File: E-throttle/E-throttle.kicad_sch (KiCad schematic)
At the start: 34 parts, among them J1 PROG, J2 JTAG, J3 Conn_01x11, J4 Conn_01x11, J5 776087-1, Q1 NMOS, SW1 SW_Push, U1 ESP32-S3-WROOM-1-N16R8, U2 LM317_SOT-223, U3 LM317_SOT-223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

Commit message: Completed wiring 2.0
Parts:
- added H1, H2, H3, H4: MountingHole_Pad, MountingHole:MountingHole_3.2mm_M3_Pad_Via, symbol Mechanical:MountingHole_Pad
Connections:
- net CAN-H: now also J5.16 (Pin_16); no longer J5.19 (Pin_19)
- net CAN-L: now also J5.17 (Pin_17); no longer J5.20 (Pin_20)
- net GND: now also J5.15 (Pin_15), J5.18 (Pin_18), J5.19 (Pin_19), H1.1, H2.1, H3.1, H4.1; no longer J5.21 (Pin_21), J5.22 (Pin_22), J5.23 (Pin_23)
- net STEP-1+: now also J5.20 (Pin_20); no longer J5.15 (Pin_15)
- net STEP-1-: now also J5.21 (Pin_21); no longer J5.16 (Pin_16)
- net STEP-2+: now also J5.22 (Pin_22); no longer J5.17 (Pin_17)
- net STEP-2-: now also J5.23 (Pin_23); no longer J5.18 (Pin_18)

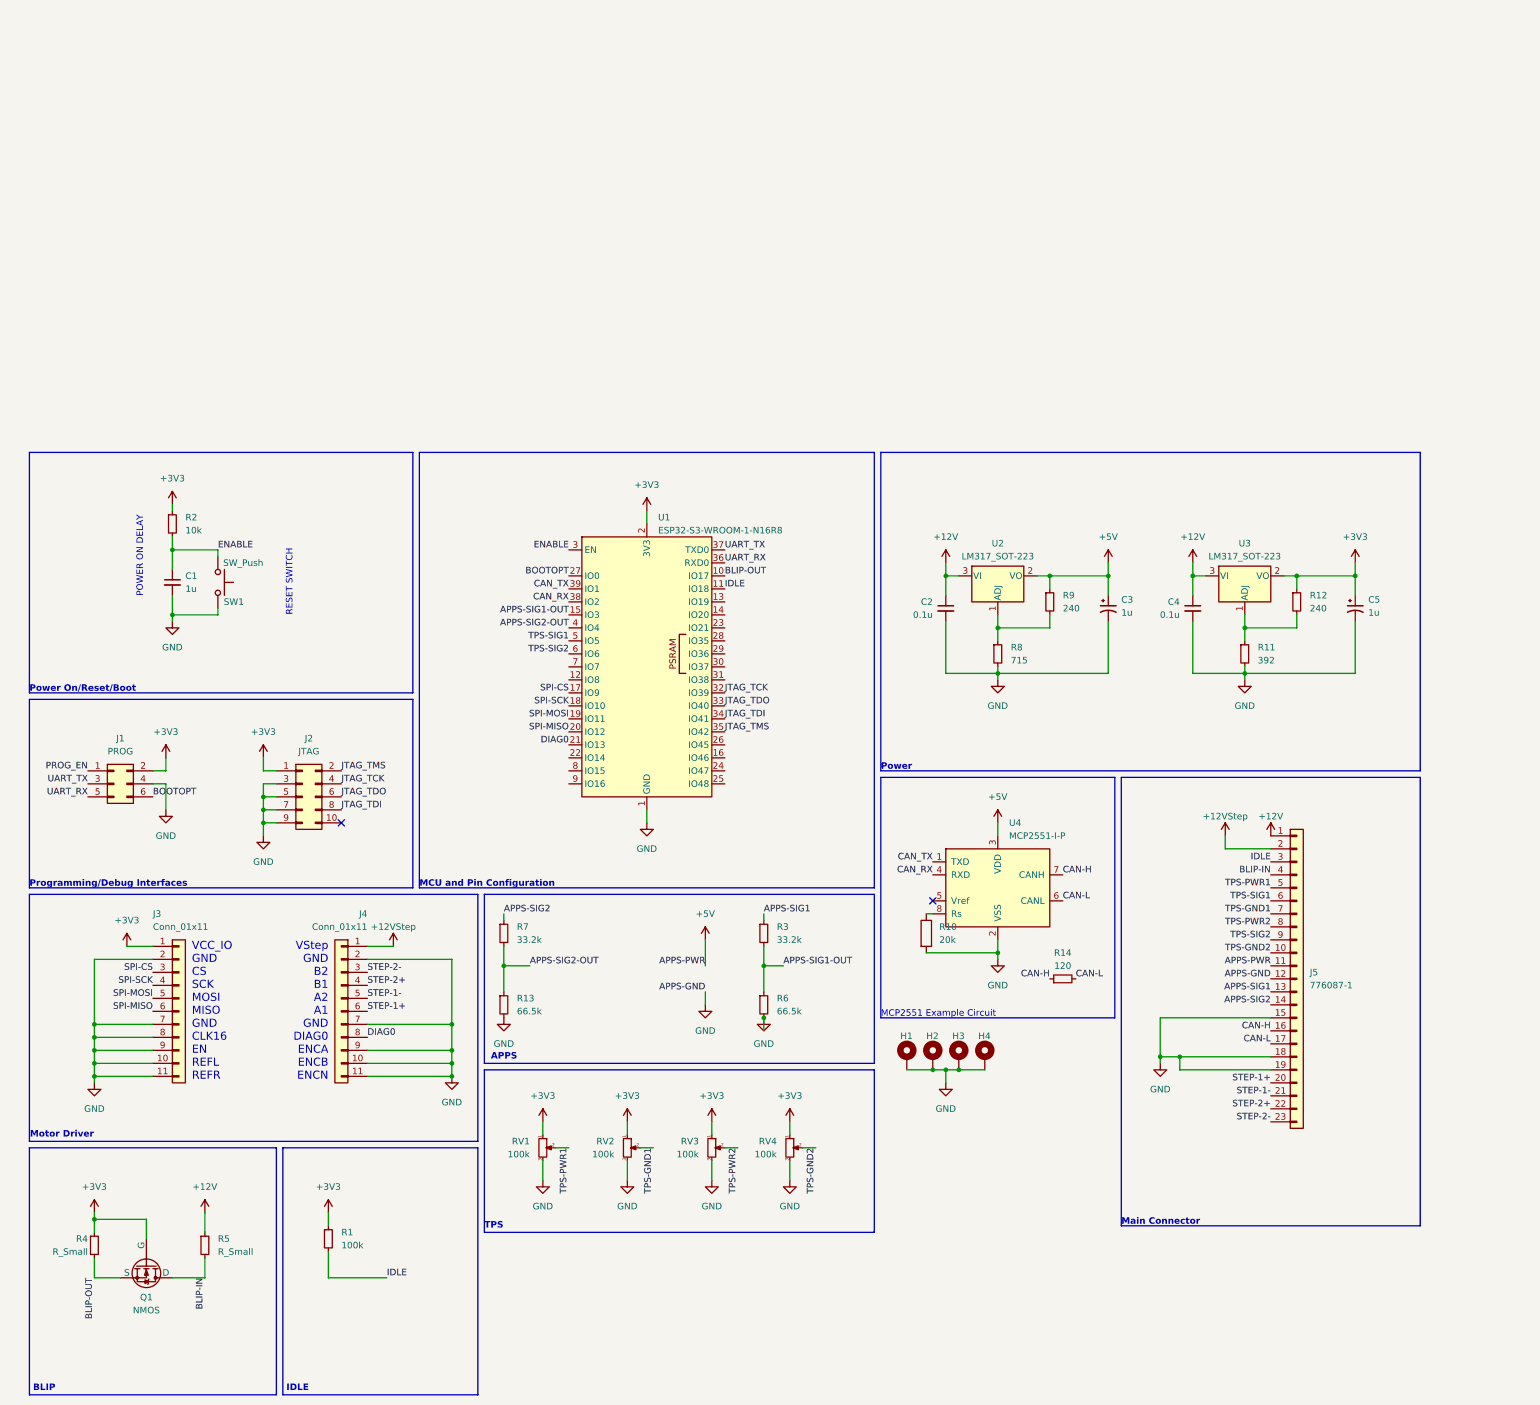
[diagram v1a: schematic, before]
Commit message: Updated PCB for 2026 (v0.1)
- Switch from ESP32 S3 Wroom1 Module to ESP dev board (Todo: Check Power Supply to ESP32 and other components)
- Fixed incorrect TPS wiring (replaced variable resistors)
- Did not reconnect JTAG debugger and programmer to ESP32 Dev Board
- Did not reconnect CAN Transceiver

Co-Authored-By: Clement Tong (Yuk Chun) <clement.yc.tong@gmail.com>
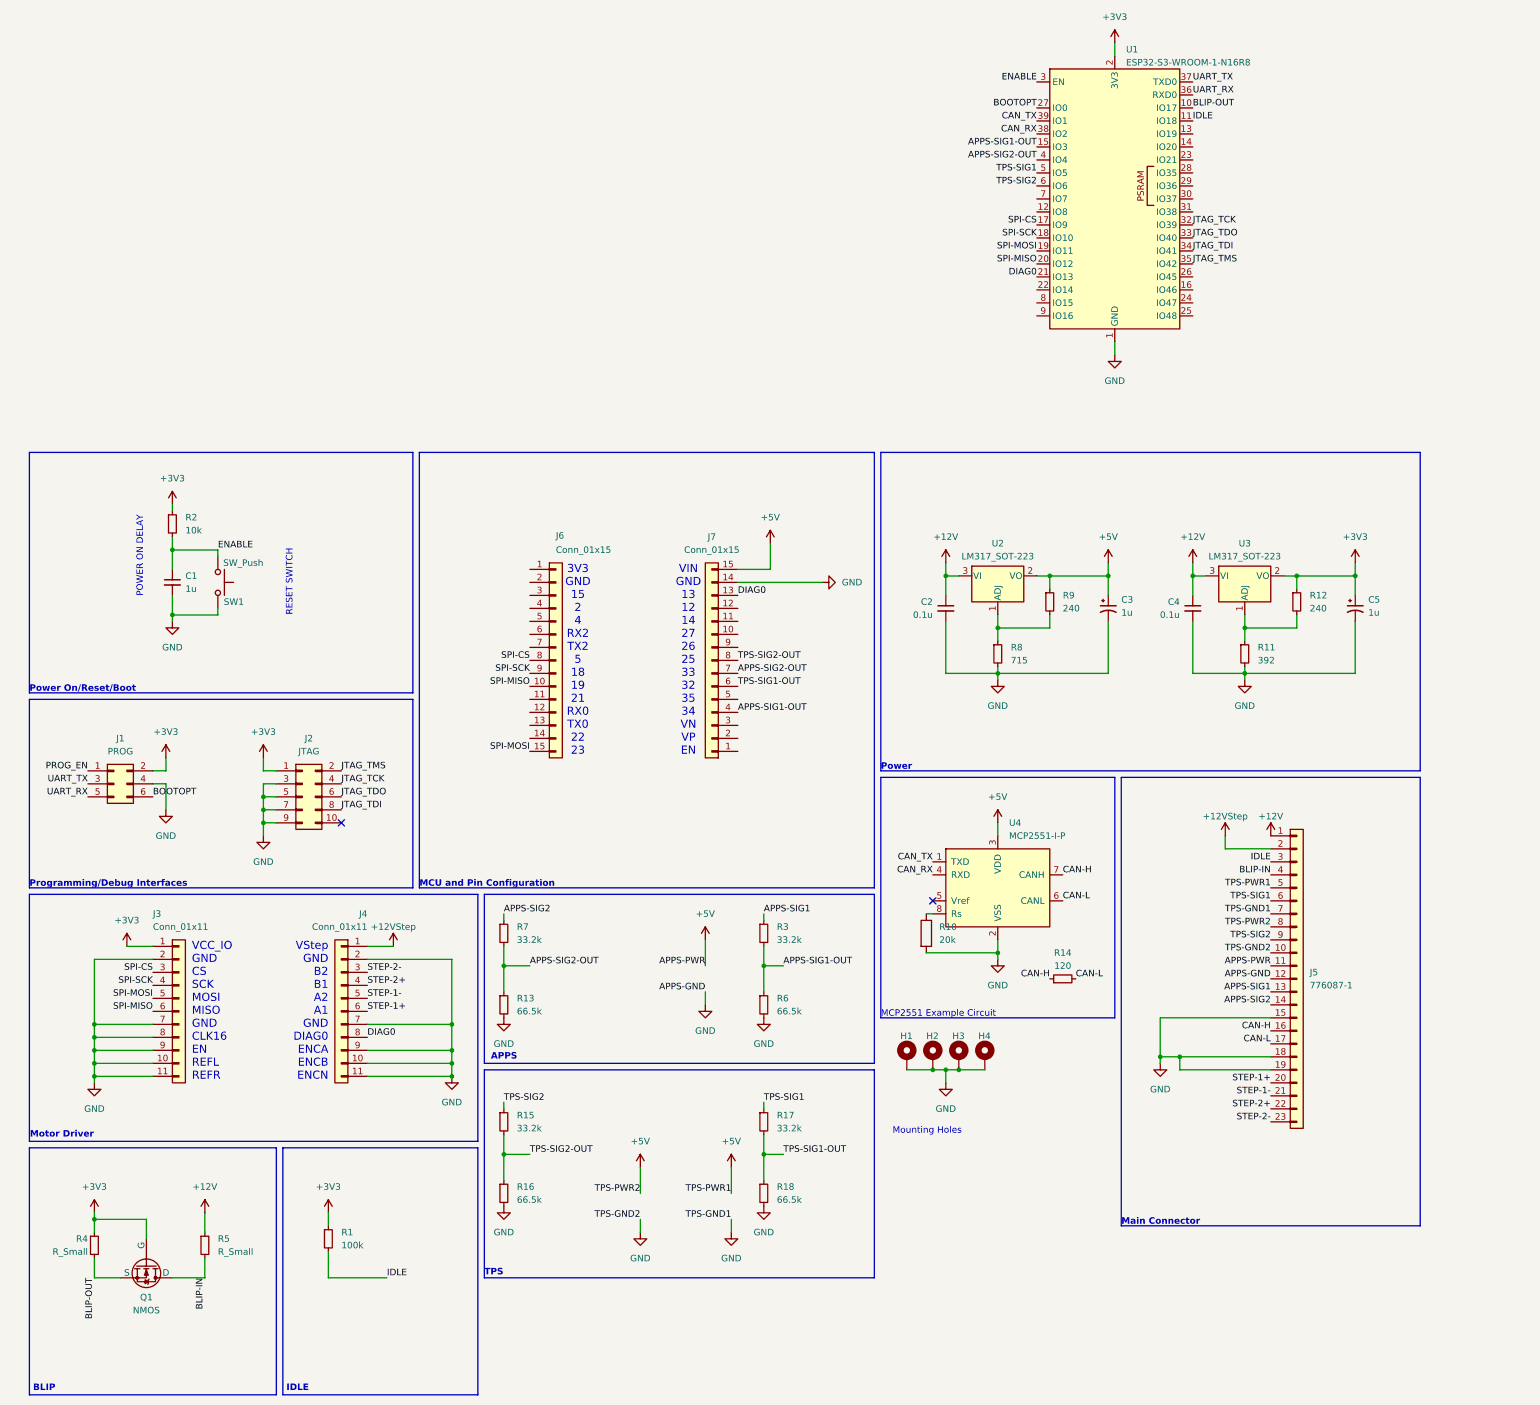
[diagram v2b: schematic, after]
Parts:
- removed RV1, RV2, RV3, RV4: 100k, Potentiometer_THT:Potentiometer_Bourns_3296Y_Vertical, symbol Device:R_Potentiometer_Small
- added J6, J7: Conn_01x15, symbol Connector_Generic:Conn_01x15
- added R15, R17: 33.2k, Resistor_THT:R_Axial_DIN0207_L6.3mm_D2.5mm_P10.16mm_Horizontal, symbol Device:R_Small
- added R16, R18: 66.5k, Resistor_THT:R_Axial_DIN0207_L6.3mm_D2.5mm_P10.16mm_Horizontal, symbol Device:R_Small
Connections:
- net TPS-GND1 is gone; now on net GND: J5.7 (Pin_7)
- net TPS-GND2 is gone; now on net GND: J5.10 (Pin_10)
- net TPS-PWR1 is gone; now on net +5V: J5.5 (Pin_5)
- net TPS-PWR2 is gone; now on net +5V: J5.8 (Pin_8)
- net +5V: now also J7.15 (Pin_15)
- net APPS-SIG1-OUT: now also J7.4 (Pin_4)
- net APPS-SIG2-OUT: now also J7.7 (Pin_7)
- net DIAG0: now also J7.13 (Pin_13)
- net GND: now also J7.14 (Pin_14), R16.2, R18.2
- net SPI-CS: now also J6.8 (Pin_8)
- net SPI-MISO: now also J6.10 (Pin_10)
- net SPI-MOSI: now also J6.15 (Pin_15)
- net SPI-SCK: now also J6.9 (Pin_9)
- net TPS-SIG1: now also R17.1
- net TPS-SIG2: now also R15.1
- new net TPS-SIG1-OUT: J7.6 (Pin_6), R17.2, R18.1
- new net TPS-SIG2-OUT: J7.8 (Pin_8), R15.2, R16.1
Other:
- note added: "3V3 GND 15 2 4 RX2 TX2 5 18 19 21 RX0 TX0 22 23"
- note added: "Mounting Holes"
- note added: "VIN GND 13 12 14 27 26 25 33 32 35 34 VN VP EN"
- moved on the sheet: U1

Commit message: Implemented Level 1 Failure Circuit
- Added Hardware Watchdog (74HC123) that requires ESP32 to send "Heartbeat" alive signal every 20ms, or else the stepper motor power gets cut

- ⁠Added PROFET / Automotive Smart High-Side Switch (BTS441TG) to cut power to the stepper motor, if the hardware watchdog doesn't receive a heartbeat from the ESP32 within the required timeframe (We set this hardware timeout to 50ms to comply with the FSUK rule CV1.6.4 that requires motor power to be cut if plausibility fails for more than 100ms)

Co-Authored-By: Clement Tong (Yuk Chun) <clement.yc.tong@gmail.com>
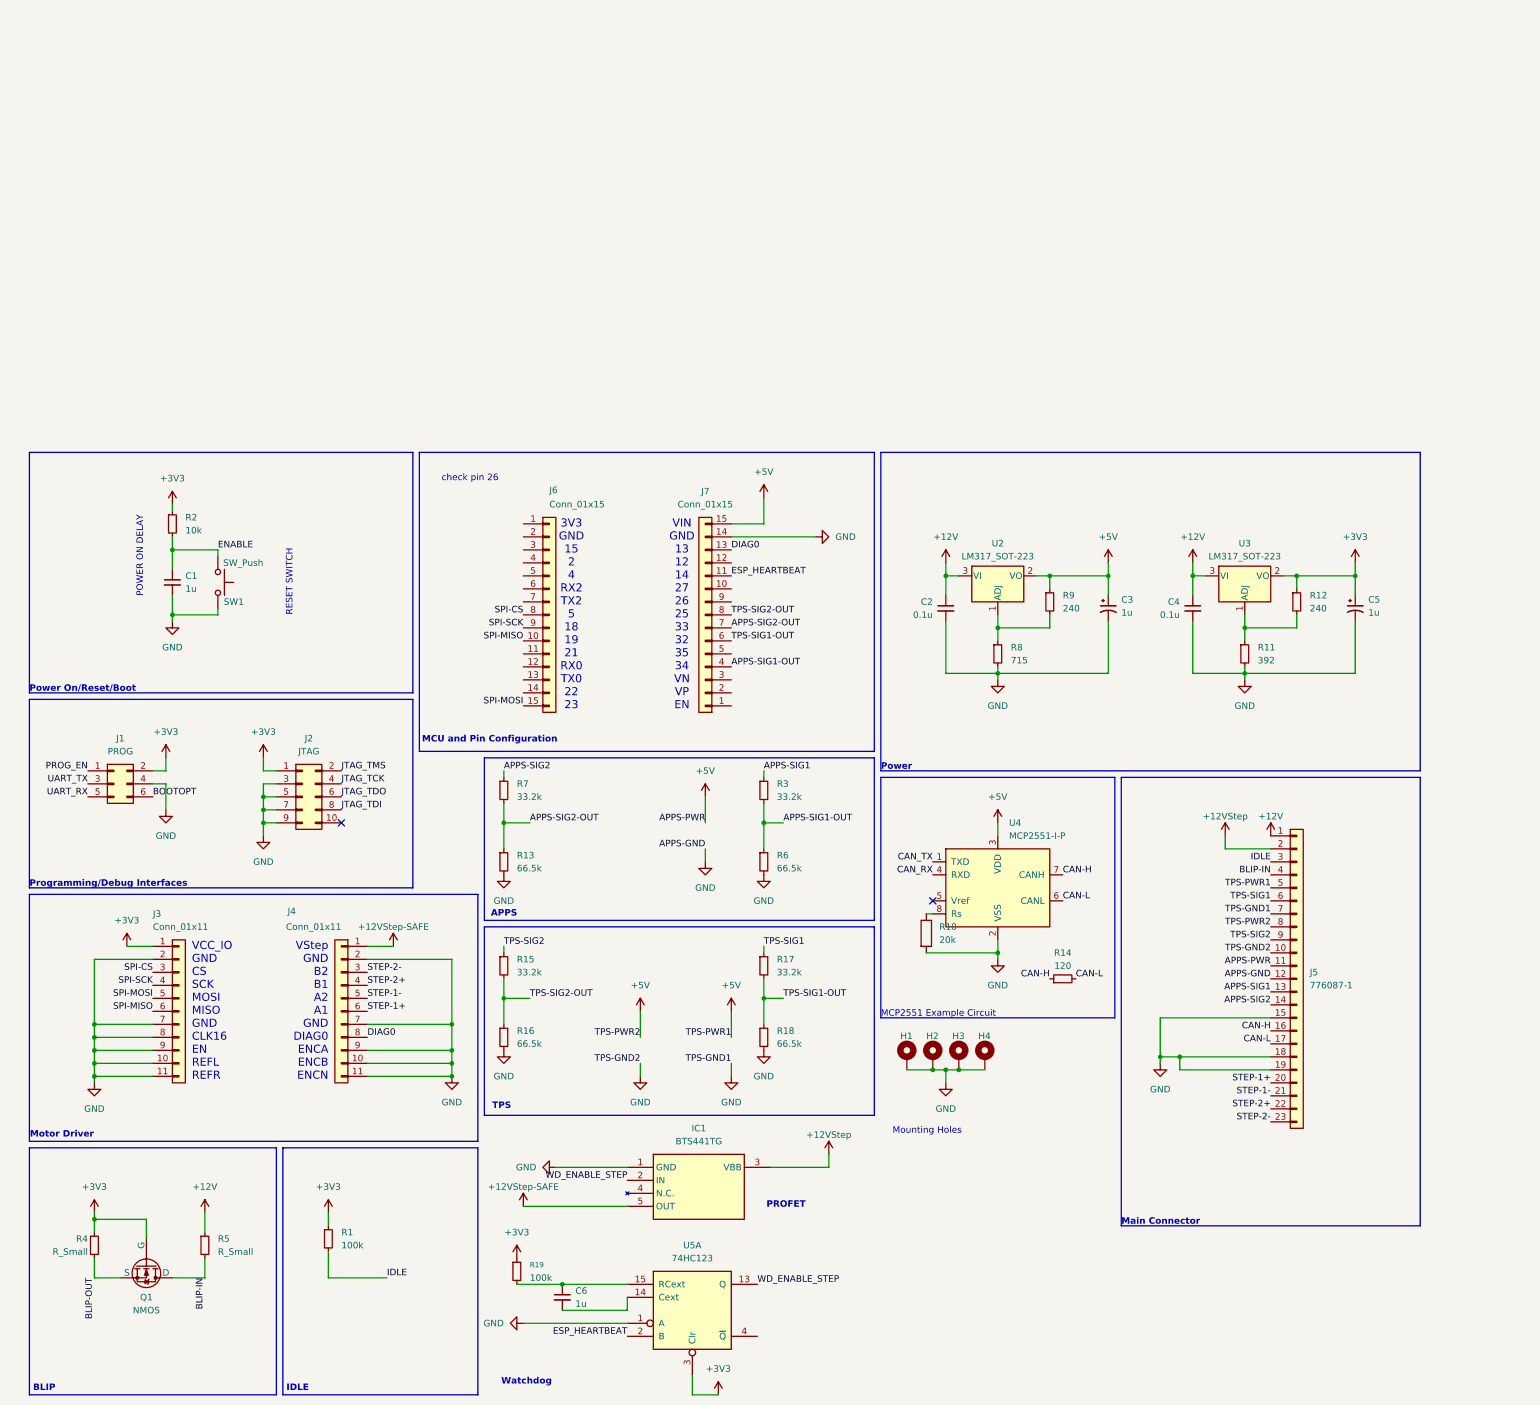
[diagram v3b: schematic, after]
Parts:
- removed U1: ESP32-S3-WROOM-1-N16R8, RF_Module:ESP32-S3-WROOM-1, symbol RF_Module:ESP32-S3-WROOM-1
- added C6: 1u, Capacitor_THT:C_Disc_D5.0mm_W2.5mm_P2.50mm, symbol Device:C_Small
- added IC1: BTS441TG, BTS441TG, symbol BTS441TG:BTS441TG
- added R19: 100k, Resistor_THT:R_Axial_DIN0207_L6.3mm_D2.5mm_P10.16mm_Horizontal, symbol Device:R_Small
- added U5: 74HC123, symbol 74xx:74HC123
- J6, J7: footprint (none) -> Connector_PinSocket_2.54mm:PinSocket_1x15_P2.54mm_Vertical
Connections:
- net +12VStep: now also IC1.3 (VBB); no longer J4.1 (Pin_1)
- net +3V3: now also R19.1, U5.3 (Clr)
- net GND: now also IC1.1 (GND), U5.1 (A)
- net ESP_HEARTBEAT: now reaches J7.11 (Pin_11)
- net ESP_HEARTBEAT: now also U5.2 (B)
- new net: C6.1, R19.2, U5.15 (RCext)
- new net: C6.2, U5.14 (Cext)
- new net +12VStep-SAFE: IC1.5 (OUT), J4.1 (Pin_1)
- new net WD_ENABLE_STEP: IC1.2 (IN), U5.13 (Q)
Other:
- note added: "PROFET"
- note added: "Watchdog"
- note added: "check pin 26"
- moved on the sheet: J6, J7, R13, R15, R16, R17, R18, R3, R6, R7
